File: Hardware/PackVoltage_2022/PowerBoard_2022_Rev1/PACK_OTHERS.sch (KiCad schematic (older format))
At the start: 20 parts, among them Q2 BUK7M8R5-40HX, Q3 BUK7M8R5-40HX, U2 LT1910, U4 INA281, U5 LT1910, U6 INA281

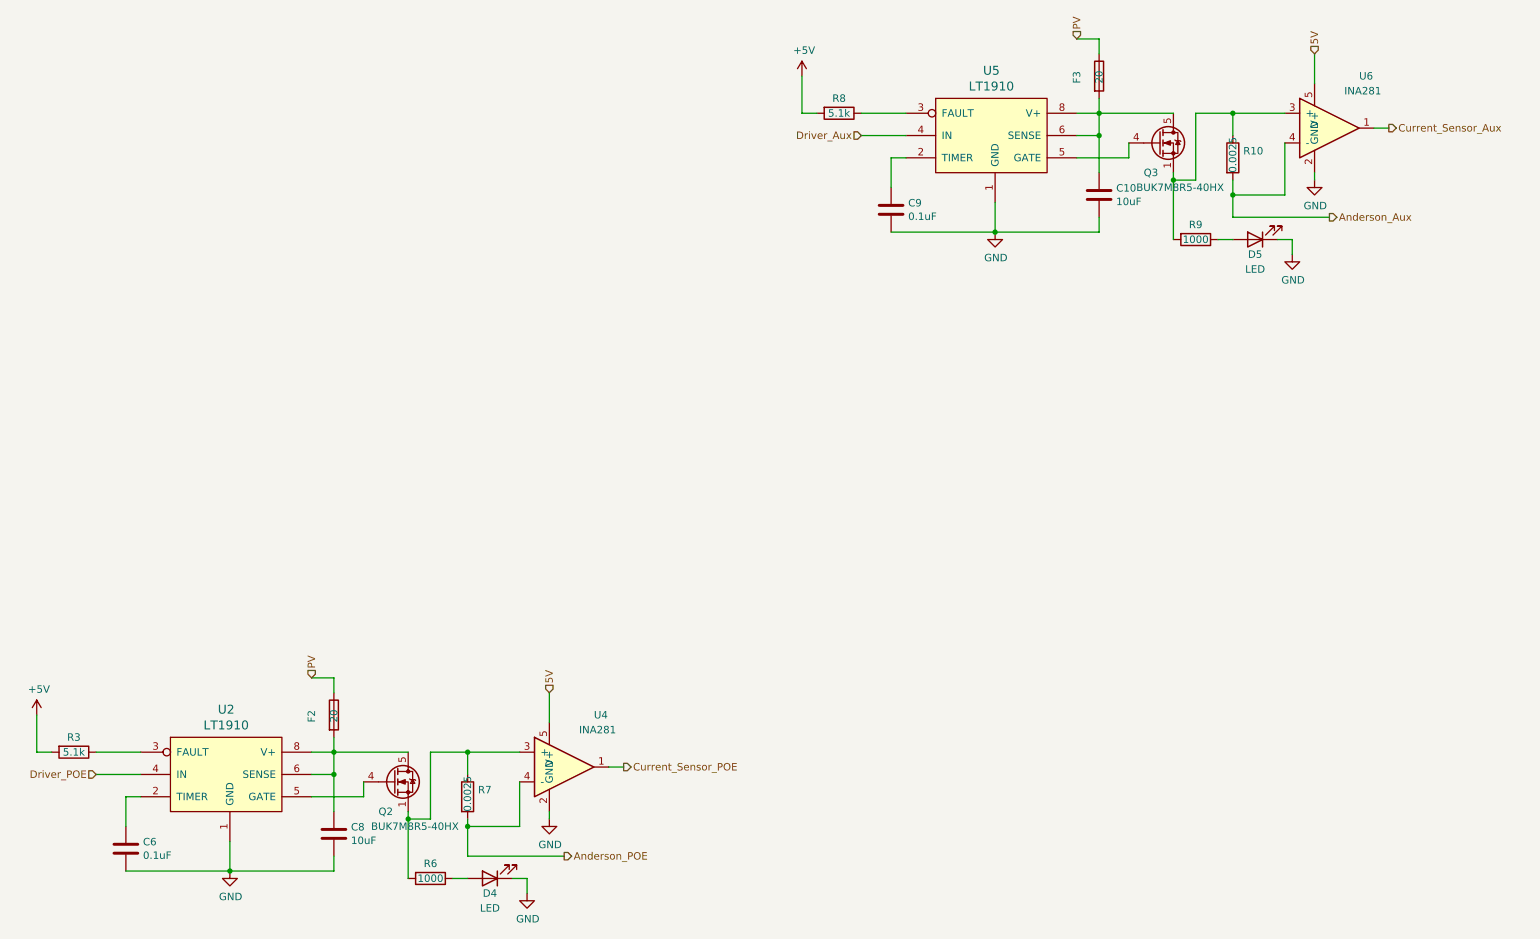
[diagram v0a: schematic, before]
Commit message: Made it to layout, found out about gnd via
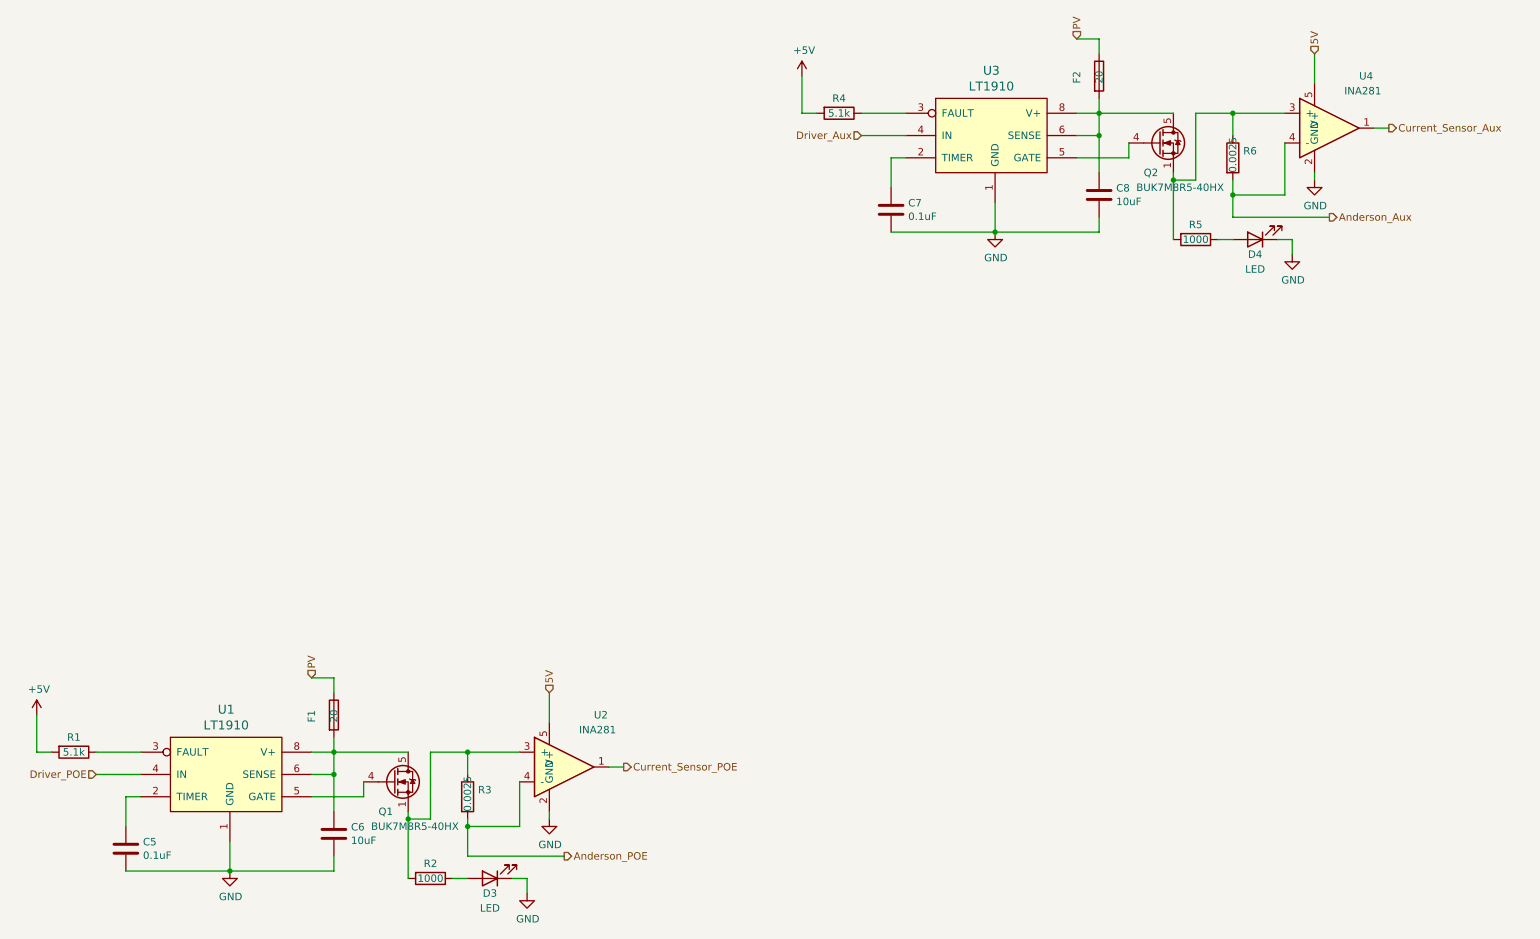
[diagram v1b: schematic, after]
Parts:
- renumbered C6 to C5, C8 to C6, C9 to C7, C10 to C8, D4 to D3, D5 to D4, F2 to F1, F3 to F2, Q2 to Q1, Q3 to Q2, R3 to R1, R6 to R2, R7 to R3, R8 to R4, R9 to R5, R10 to R6, U2 to U1, U4 to U2, U5 to U3, U6 to U4
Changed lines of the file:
@@
 P 7150 2100
 AR Path="/615D5992/61612B13" Ref="U?"  Part="1"
-AR Path="/61609A41/61612B13" Ref="U5"  Part="1"
-F 0 "U5" H 7525 2787 60  0000 C CNN
+AR Path="/61609A41/61612B13" Ref="U3"  Part="1"
+F 0 "U3" H 7525 2787 60  0000 C CNN
 F 1 "LT1910" H 7525 2681 60  0000 C CNN
 F 2 "Package_SO:SOIC-8_3.9x4.9mm_P1.27mm" H 7150 2100 60  0001 C CNN
@@
 P 6500 1700
 AR Path="/615D5992/61612B19" Ref="R?"  Part="1"
-AR Path="/61609A41/61612B19" Ref="R8"  Part="1"
-F 0 "R8" V 6400 1700 50  0000 C CNN
+AR Path="/61609A41/61612B19" Ref="R4"  Part="1"
+F 0 "R4" V 6400 1700 50  0000 C CNN
 F 1 "5.1k" V 6500 1700 50  0000 C CNN
 F 2 "Resistor_SMD:R_0603_1608Metric_Pad1.05x0.95mm_HandSolder" V 6430 1700 50  0001 C CNN
@@
 P 6250 1450
 AR Path="/615D5992/61612B20" Ref="#PWR?"  Part="1"
-AR Path="/61609A41/61612B20" Ref="#PWR0102"  Part="1"
-F 0 "#PWR0102" H 6250 1300 50  0001 C CNN
+AR Path="/61609A41/61612B20" Ref="#PWR06"  Part="1"
+F 0 "#PWR06" H 6250 1300 50  0001 C CNN
 F 1 "+5V" H 6265 1623 50  0000 C CNN
 F 2 "" H 6250 1450 50  0001 C CNN
@@
 P 6850 2350
 AR Path="/615D5992/61612B28" Ref="C?"  Part="1"
-AR Path="/61609A41/61612B28" Ref="C9"  Part="1"
-F 0 "C9" H 6965 2396 50  0000 L CNN
+AR Path="/61609A41/61612B28" Ref="C7"  Part="1"
+F 0 "C7" H 6965 2396 50  0000 L CNN
 F 1 "0.1uF" H 6965 2305 50  0000 L CNN
 F 2 "Capacitor_SMD:C_0603_1608Metric_Pad1.05x0.95mm_HandSolder" H 6888 2200 50  0001 C CNN
@@
 P 7550 2500
 AR Path="/615D5992/61612B30" Ref="#PWR?"  Part="1"
-AR Path="/61609A41/61612B30" Ref="#PWR0103"  Part="1"
-F 0 "#PWR0103" H 7550 2250 50  0001 C CNN
+AR Path="/61609A41/61612B30" Ref="#PWR07"  Part="1"
+F 0 "#PWR07" H 7550 2250 50  0001 C CNN
 F 1 "GND" H 7555 2327 50  0000 C CNN
 F 2 "" H 7550 2500 50  0001 C CNN
@@
 P 8250 1450
 AR Path="/615D5992/61612B36" Ref="F?"  Part="1"
-AR Path="/61609A41/61612B36" Ref="F3"  Part="1"
-F 0 "F3" V 8100 1400 50  0000 L CNN
+AR Path="/61609A41/61612B36" Ref="F2"  Part="1"
+F 0 "F2" V 8100 1400 50  0000 L CNN
 F 1 "20" V 8250 1400 50  0000 L CNN
 F 2 "Fuse:Fuse_0603_1608Metric_Pad1.05x0.95mm_HandSolder" V 8180 1450 50  0001 C CNN
@@
 P 8250 2250
 AR Path="/615D5992/61612B4D" Ref="C?"  Part="1"
-AR Path="/61609A41/61612B4D" Ref="C10"  Part="1"
-F 0 "C10" H 8365 2296 50  0000 L CNN
+AR Path="/61609A41/61612B4D" Ref="C8"  Part="1"
+F 0 "C8" H 8365 2296 50  0000 L CNN
 F 1 "10uF" H 8365 2205 50  0000 L CNN
 F 2 "Capacitor_SMD:C_0603_1608Metric_Pad1.05x0.95mm_HandSolder" H 8288 2100 50  0001 C CNN
@@
 P 8900 2550
 AR Path="/615D5992/61612B53" Ref="R?"  Part="1"
-AR Path="/61609A41/61612B53" Ref="R9"  Part="1"
-F 0 "R9" V 8800 2550 50  0000 C CNN
+AR Path="/61609A41/61612B53" Ref="R5"  Part="1"
+F 0 "R5" V 8800 2550 50  0000 C CNN
 F 1 "1000" V 8900 2550 50  0000 C CNN
 F 2 "Resistor_SMD:R_0603_1608Metric_Pad1.05x0.95mm_HandSolder" V 8830 2550 50  0001 C CNN
@@
 P 9300 2550
 AR Path="/615D5992/61612B59" Ref="D?"  Part="1"
-AR Path="/61609A41/61612B59" Ref="D5"  Part="1"
-F 0 "D5" H 9300 2650 50  0000 C CNN
+AR Path="/61609A41/61612B59" Ref="D4"  Part="1"
+F 0 "D4" H 9300 2650 50  0000 C CNN
 F 1 "LED" H 9300 2750 50  0000 C CNN
 F 2 "LED_SMD:LED_0603_1608Metric_Pad1.05x0.95mm_HandSolder" H 9300 2550 50  0001 C CNN
@@
 P 9550 2650
 AR Path="/615D5992/61612B5F" Ref="#PWR?"  Part="1"
-AR Path="/61609A41/61612B5F" Ref="#PWR0104"  Part="1"
-F 0 "#PWR0104" H 9550 2400 50  0001 C CNN
+AR Path="/61609A41/61612B5F" Ref="#PWR08"  Part="1"
+F 0 "#PWR08" H 9550 2400 50  0001 C CNN
 F 1 "GND" H 9555 2477 50  0000 C CNN
 F 2 "" H 9550 2650 50  0001 C CNN
@@
 P 9700 1800
 AR Path="/615D5992/61612B67" Ref="U?"  Part="1"
-AR Path="/61609A41/61612B67" Ref="U6"  Part="1"
-F 0 "U6" H 10000 2150 50  0000 L CNN
+AR Path="/61609A41/61612B67" Ref="U4"  Part="1"
+F 0 "U4" H 10000 2150 50  0000 L CNN
 F 1 "INA281" H 9900 2050 50  0000 L CNN
 F 2 "Package_TO_SOT_SMD:SOT-23-5" H 9950 2000 50  0001 C CNN
@@
 P 9150 2000
 AR Path="/615D5992/61612B6D" Ref="R?"  Part="1"
-AR Path="/61609A41/61612B6D" Ref="R10"  Part="1"
-F 0 "R10" H 9220 2046 50  0000 L CNN
+AR Path="/61609A41/61612B6D" Ref="R6"  Part="1"
+F 0 "R6" H 9220 2046 50  0000 L CNN
 F 1 "0.0025" V 9150 1900 50  0000 L CNN
 F 2 "Resistor_SMD:R_0603_1608Metric_Pad1.05x0.95mm_HandSolder" V 9080 2000 50  0001 C CNN
@@
 P 9700 2150
 AR Path="/615D5992/61612B75" Ref="#PWR?"  Part="1"
-AR Path="/61609A41/61612B75" Ref="#PWR0105"  Part="1"
-F 0 "#PWR0105" H 9700 1900 50  0001 C CNN
+AR Path="/61609A41/61612B75" Ref="#PWR09"  Part="1"
+F 0 "#PWR09" H 9700 1900 50  0001 C CNN
 F 1 "GND" H 9705 1977 50  0000 C CNN
 F 2 "" H 9700 2150 50  0001 C CNN
@@
 P 2000 6400
 AR Path="/615D5992/616288AA" Ref="U?"  Part="1"
-AR Path="/61609A41/616288AA" Ref="U2"  Part="1"
-F 0 "U2" H 2375 7087 60  0000 C CNN
+AR Path="/61609A41/616288AA" Ref="U1"  Part="1"
+F 0 "U1" H 2375 7087 60  0000 C CNN
 F 1 "LT1910" H 2375 6981 60  0000 C CNN
 F 2 "Package_SO:SOIC-8_3.9x4.9mm_P1.27mm" H 2000 6400 60  0001 C CNN
@@
 P 1350 6000
 AR Path="/615D5992/616288B0" Ref="R?"  Part="1"
-AR Path="/61609A41/616288B0" Ref="R3"  Part="1"
-F 0 "R3" V 1250 6000 50  0000 C CNN
+AR Path="/61609A41/616288B0" Ref="R1"  Part="1"
+F 0 "R1" V 1250 6000 50  0000 C CNN
 F 1 "5.1k" V 1350 6000 50  0000 C CNN
 F 2 "Resistor_SMD:R_0603_1608Metric_Pad1.05x0.95mm_HandSolder" V 1280 6000 50  0001 C CNN
@@
 P 1100 5750
 AR Path="/615D5992/616288B7" Ref="#PWR?"  Part="1"
-AR Path="/61609A41/616288B7" Ref="#PWR0110"  Part="1"
-F 0 "#PWR0110" H 1100 5600 50  0001 C CNN
+AR Path="/61609A41/616288B7" Ref="#PWR02"  Part="1"
+F 0 "#PWR02" H 1100 5600 50  0001 C CNN
 F 1 "+5V" H 1115 5923 50  0000 C CNN
 F 2 "" H 1100 5750 50  0001 C CNN
@@
 P 1700 6650
 AR Path="/615D5992/616288BF" Ref="C?"  Part="1"
-AR Path="/61609A41/616288BF" Ref="C6"  Part="1"
-F 0 "C6" H 1815 6696 50  0000 L CNN
+AR Path="/61609A41/616288BF" Ref="C5"  Part="1"
+F 0 "C5" H 1815 6696 50  0000 L CNN
 F 1 "0.1uF" H 1815 6605 50  0000 L CNN
 F 2 "Capacitor_SMD:C_0603_1608Metric_Pad1.05x0.95mm_HandSolder" H 1738 6500 50  0001 C CNN
@@
 P 2400 6800
 AR Path="/615D5992/616288C7" Ref="#PWR?"  Part="1"
-AR Path="/61609A41/616288C7" Ref="#PWR0111"  Part="1"
-F 0 "#PWR0111" H 2400 6550 50  0001 C CNN
+AR Path="/61609A41/616288C7" Ref="#PWR03"  Part="1"
+F 0 "#PWR03" H 2400 6550 50  0001 C CNN
 F 1 "GND" H 2405 6627 50  0000 C CNN
 F 2 "" H 2400 6800 50  0001 C CNN
@@
 P 3100 5750
 AR Path="/615D5992/616288CD" Ref="F?"  Part="1"
-AR Path="/61609A41/616288CD" Ref="F2"  Part="1"
-F 0 "F2" V 2950 5700 50  0000 L CNN
+AR Path="/61609A41/616288CD" Ref="F1"  Part="1"
+F 0 "F1" V 2950 5700 50  0000 L CNN
 F 1 "20" V 3100 5700 50  0000 L CNN
 F 2 "Fuse:Fuse_0603_1608Metric_Pad1.05x0.95mm_HandSolder" V 3030 5750 50  0001 C CNN
@@
 P 3500 6200
 AR Path="/615D5992/616288D7" Ref="Q?"  Part="1"
-AR Path="/61609A41/616288D7" Ref="Q2"  Part="1"
-F 0 "Q2" H 3400 6000 50  0000 L CNN
+AR Path="/61609A41/616288D7" Ref="Q1"  Part="1"
+F 0 "Q1" H 3400 6000 50  0000 L CNN
 F 1 "BUK7M8R5-40HX" H 3350 5900 50  0000 L CNN
 F 2 "Package_TO_SOT_SMD:LFPAK33" H 3700 6125 50  0001 L CIN
@@
 P 3100 6550
 AR Path="/615D5992/616288E4" Ref="C?"  Part="1"
-AR Path="/61609A41/616288E4" Ref="C8"  Part="1"
-F 0 "C8" H 3215 6596 50  0000 L CNN
+AR Path="/61609A41/616288E4" Ref="C6"  Part="1"
+F 0 "C6" H 3215 6596 50  0000 L CNN
 F 1 "10uF" H 3215 6505 50  0000 L CNN
 F 2 "Capacitor_SMD:C_0603_1608Metric_Pad1.05x0.95mm_HandSolder" H 3138 6400 50  0001 C CNN
@@
 P 3750 6850
 AR Path="/615D5992/616288EA" Ref="R?"  Part="1"
-AR Path="/61609A41/616288EA" Ref="R6"  Part="1"
-F 0 "R6" V 3650 6850 50  0000 C CNN
+AR Path="/61609A41/616288EA" Ref="R2"  Part="1"
+F 0 "R2" V 3650 6850 50  0000 C CNN
 F 1 "1000" V 3750 6850 50  0000 C CNN
 F 2 "Resistor_SMD:R_0603_1608Metric_Pad1.05x0.95mm_HandSolder" V 3680 6850 50  0001 C CNN
@@
 P 4150 6850
 AR Path="/615D5992/616288F0" Ref="D?"  Part="1"
-AR Path="/61609A41/616288F0" Ref="D4"  Part="1"
-F 0 "D4" H 4150 6950 50  0000 C CNN
+AR Path="/61609A41/616288F0" Ref="D3"  Part="1"
+F 0 "D3" H 4150 6950 50  0000 C CNN
 F 1 "LED" H 4150 7050 50  0000 C CNN
 F 2 "LED_SMD:LED_0603_1608Metric_Pad1.05x0.95mm_HandSolder" H 4150 6850 50  0001 C CNN
@@
 P 4400 6950
 AR Path="/615D5992/616288F6" Ref="#PWR?"  Part="1"
-AR Path="/61609A41/616288F6" Ref="#PWR0112"  Part="1"
-F 0 "#PWR0112" H 4400 6700 50  0001 C CNN
+AR Path="/61609A41/616288F6" Ref="#PWR04"  Part="1"
+F 0 "#PWR04" H 4400 6700 50  0001 C CNN
 F 1 "GND" H 4405 6777 50  0000 C CNN
 F 2 "" H 4400 6950 50  0001 C CNN
@@
 P 4550 6100
 AR Path="/615D5992/616288FE" Ref="U?"  Part="1"
-AR Path="/61609A41/616288FE" Ref="U4"  Part="1"
-F 0 "U4" H 4850 6450 50  0000 L CNN
+AR Path="/61609A41/616288FE" Ref="U2"  Part="1"
+F 0 "U2" H 4850 6450 50  0000 L CNN
 F 1 "INA281" H 4750 6350 50  0000 L CNN
 F 2 "Package_TO_SOT_SMD:SOT-23-5" H 4800 6300 50  0001 C CNN
@@
 P 4000 6300
 AR Path="/615D5992/61628904" Ref="R?"  Part="1"
-AR Path="/61609A41/61628904" Ref="R7"  Part="1"
-F 0 "R7" H 4070 6346 50  0000 L CNN
+AR Path="/61609A41/61628904" Ref="R3"  Part="1"
+F 0 "R3" H 4070 6346 50  0000 L CNN
 F 1 "0.0025" V 4000 6200 50  0000 L CNN
 F 2 "Resistor_SMD:R_0603_1608Metric_Pad1.05x0.95mm_HandSolder" V 3930 6300 50  0001 C CNN
@@
 P 4550 6450
 AR Path="/615D5992/6162890C" Ref="#PWR?"  Part="1"
-AR Path="/61609A41/6162890C" Ref="#PWR0113"  Part="1"
-F 0 "#PWR0113" H 4550 6200 50  0001 C CNN
+AR Path="/61609A41/6162890C" Ref="#PWR05"  Part="1"
+F 0 "#PWR05" H 4550 6200 50  0001 C CNN
 F 1 "GND" H 4555 6277 50  0000 C CNN
 F 2 "" H 4550 6450 50  0001 C CNN
@@
 P 8650 1900
 AR Path="/615D5992/61612B40" Ref="Q?"  Part="1"
-AR Path="/61609A41/61612B40" Ref="Q3"  Part="1"
-F 0 "Q3" H 8550 1700 50  0000 L CNN
+AR Path="/61609A41/61612B40" Ref="Q2"  Part="1"
+F 0 "Q2" H 8550 1700 50  0000 L CNN
 F 1 "BUK7M8R5-40HX" H 8500 1600 50  0000 L CNN
 F 2 "Package_TO_SOT_SMD:LFPAK33" H 8850 1825 50  0001 L CIN

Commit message: fixed Fuses
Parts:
- F1, F2: footprint Fuse:Fuse_0603_1608Metric_Pad1.05x0.95mm_HandSolder -> MRDT_Passives:ATC_Fuse_Block
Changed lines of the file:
@@
 F 0 "F2" V 8100 1400 50  0000 L CNN
 F 1 "20" V 8250 1400 50  0000 L CNN
-F 2 "Fuse:Fuse_0603_1608Metric_Pad1.05x0.95mm_HandSolder" V 8180 1450 50  0001 C CNN
+F 2 "MRDT_Passives:ATC_Fuse_Block" V 8180 1450 50  0001 C CNN
 F 3 "~" H 8250 1450 50  0001 C CNN
 	1    8250 1450
@@
 F 0 "F1" V 2950 5700 50  0000 L CNN
 F 1 "20" V 3100 5700 50  0000 L CNN
-F 2 "Fuse:Fuse_0603_1608Metric_Pad1.05x0.95mm_HandSolder" V 3030 5750 50  0001 C CNN
+F 2 "MRDT_Passives:ATC_Fuse_Block" V 3030 5750 50  0001 C CNN
 F 3 "~" H 3100 5750 50  0001 C CNN
 	1    3100 5750
